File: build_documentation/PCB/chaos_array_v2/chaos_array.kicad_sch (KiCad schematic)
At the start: 26 parts, among them SW1 RotaryEncoder_Switch, SW2 SW_Push, SW3 RotaryEncoder_Switch, SW4 SW_Push, SW5 RotaryEncoder_Switch, SW6 SW_Push, SW7 RotaryEncoder_Switch, SW8 SW_Push, U1 RP2040-Zero

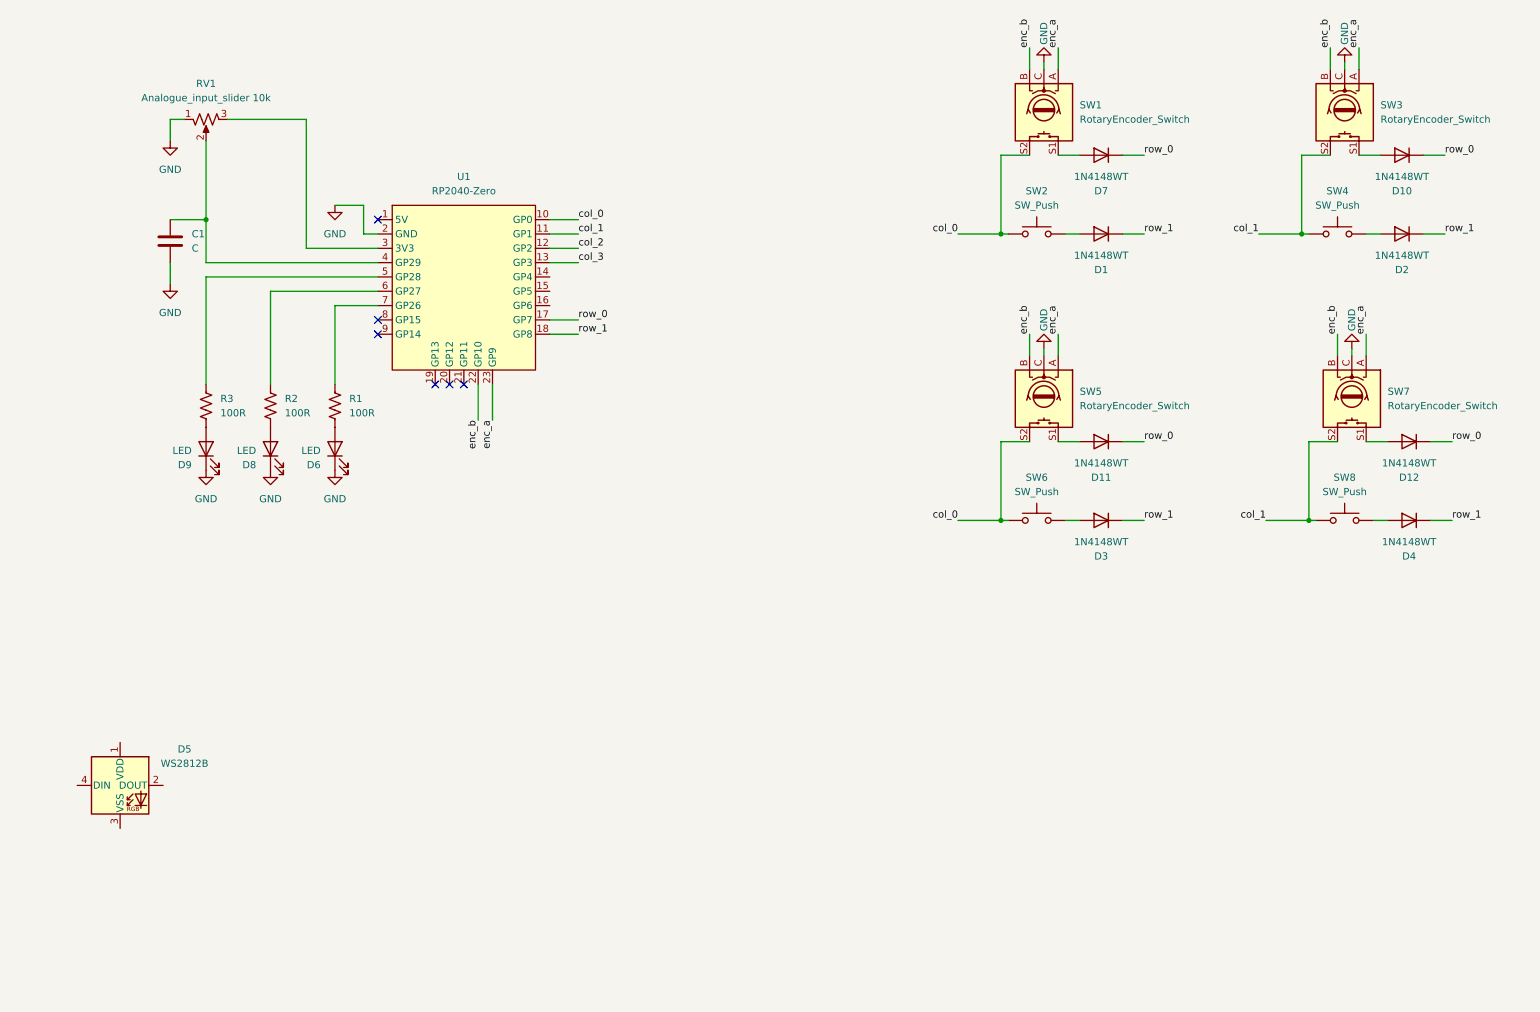
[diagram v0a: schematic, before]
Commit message: Create LED array and breakout area
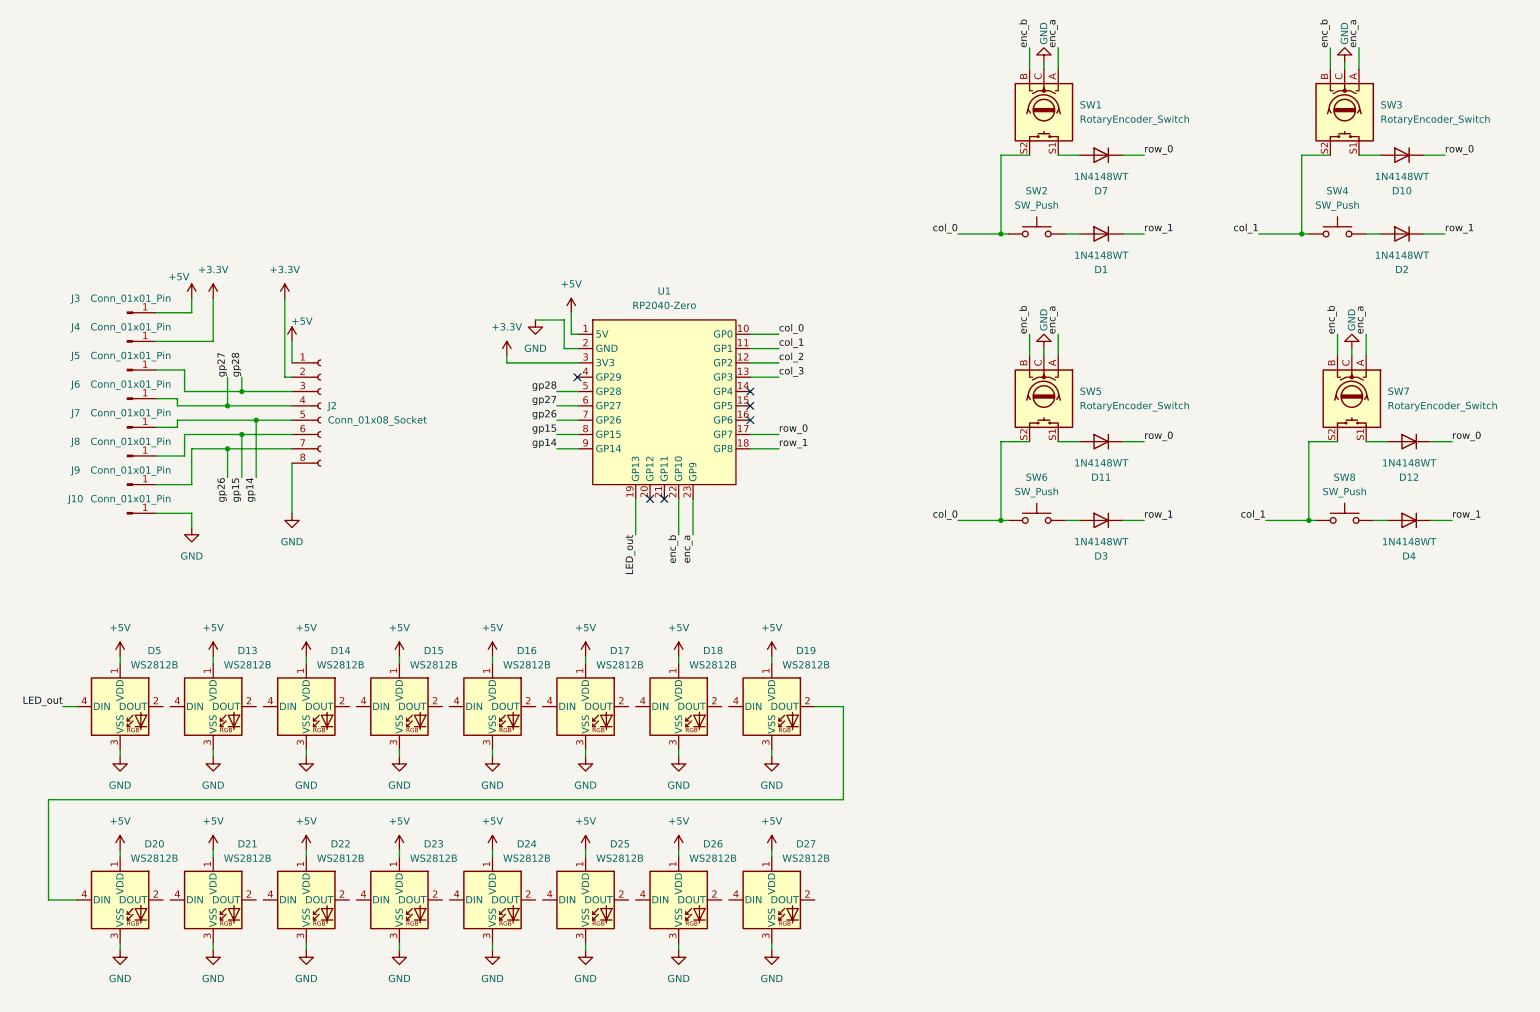
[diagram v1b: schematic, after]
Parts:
- removed C1: C, Capacitor_THT:C_Disc_D5.0mm_W2.5mm_P5.00mm, symbol Device:C
- removed D6, D8, D9: LED, LED_THT:LED_D3.0mm, symbol Device:LED
- removed R1, R2, R3: 100R, Resistor_THT:R_Axial_DIN0204_L3.6mm_D1.6mm_P5.08mm_Horizontal, symbol Device:R_US
- removed RV1: Analogue_input_slider 10k, CustomFootprints:Potentiometer_slide_75mm_range_60mm_2_sets, symbol Device:R_Potentiometer_US
- added D13, D14, D15, D16, D17, D18, D19, D20, D21, D22, D23, D24, D25, D26, D27: WS2812B, LED_SMD:LED_WS2812B_PLCC4_5.0x5.0mm_P3.2mm, symbol LED:WS2812B
- added J10, J3, J4, J5, J6, J7, J8, J9: Conn_01x01_Pin, symbol Connector:Conn_01x01_Pin
- added J2: Conn_01x08_Socket, Connector_JST:JST_EH_B8B-EH-A_1x08_P2.50mm_Vertical, symbol Connector:Conn_01x08_Socket
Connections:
- net GND: now also D5.3 (VSS), D13.3 (VSS), D14.3 (VSS), D15.3 (VSS), D16.3 (VSS), D17.3 (VSS), D18.3 (VSS), D19.3 (VSS), D20.3 (VSS), D21.3 (VSS), D22.3 (VSS), D23.3 (VSS), D24.3 (VSS), D25.3 (VSS), D26.3 (VSS), D27.3 (VSS), J10.1 (Pin_1), J2.8 (Pin_8)
- net +5V: now reaches U1.1 (5V)
- net +5V: now also D5.1 (VDD), D13.1 (VDD), D14.1 (VDD), D15.1 (VDD), D16.1 (VDD), D17.1 (VDD), D18.1 (VDD), D19.1 (VDD), D20.1 (VDD), D21.1 (VDD), D22.1 (VDD), D23.1 (VDD), D24.1 (VDD), D25.1 (VDD), D26.1 (VDD), D27.1 (VDD), J2.1 (Pin_1), J3.1 (Pin_1)
- net LED_out: now reaches U1.19 (GP13)
- net LED_out: now also D5.4 (DIN)
- net +3.3V: now reaches U1.3 (3V3)
- net +3.3V: now also J2.2 (Pin_2), J4.1 (Pin_1)
- net gp28: now reaches U1.5 (GP28)
- net gp28: now also J2.3 (Pin_3), J5.1 (Pin_1)
- net gp27: now reaches U1.6 (GP27)
- net gp27: now also J2.4 (Pin_4), J6.1 (Pin_1)
- net gp26: now reaches U1.7 (GP26)
- net gp26: now also J2.7 (Pin_7), J9.1 (Pin_1)
- net gp15: now reaches U1.8 (GP15)
- net gp15: now also J2.6 (Pin_6), J8.1 (Pin_1)
- net gp14: now reaches U1.9 (GP14)
- net gp14: now also J2.5 (Pin_5), J7.1 (Pin_1)
- new net: D19.2 (DOUT), D20.4 (DIN)
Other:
- moved on the sheet: D5, U1

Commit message: update BOM
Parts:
- D1, D10, D11, D2, D3, D4, D7: footprint Key_Switches:D_DO-35_SOD27_P5.08mm_Horizontal -> Diode_SMD:D_MiniMELF
- D5: renamed from D12; footprint Key_Switches:D_DO-35_SOD27_P5.08mm_Horizontal -> Diode_SMD:D_MiniMELF
- J10, J3, J4, J5, J6, J7, J8, J9: footprint (none) -> TestPoint:TestPoint_Pad_3.0x3.0mm
- renumbered D5 to D12
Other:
- note added: "WLED_array"
- note added: "breakout_area"
- note added: "switches_rotaries"
- moved on the sheet: D1, D10, D11, D12, D13, D14, D15, D16, D17, D18, D19, D2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

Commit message: Update footprints
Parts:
- SW2, SW4, SW6, SW8: footprint Key_Switches:Kailh_socket_MX_PG1350_optional -> footprints:Kailh_socket_MX_PG1350_optional
- U1: footprint CustomFootprints:RP2040 Zero -> RP2040 Zero:RP2040 Zero
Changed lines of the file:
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@@
 			)
 		)
-		(property "Footprint" "Key_Switches:Kailh_socket_MX_PG1350_optional"
+		(property "Footprint" "footprints:Kailh_socket_MX_PG1350_optional"
 			(at 251.46 147.32 0)
 			(hide yes)
@@
 			)
 		)
-		(property "Footprint" "CustomFootprints:RP2040 Zero"
+		(property "Footprint" "RP2040 Zero:RP2040 Zero"
 			(at 138.43 50.8 0)
 			(hide yes)
@@
 			)
 		)
-		(property "Footprint" "Key_Switches:Kailh_socket_MX_PG1350_optional"
+		(property "Footprint" "footprints:Kailh_socket_MX_PG1350_optional"
 			(at 196.85 147.32 0)
 			(hide yes)
@@
 			)
 		)
-		(property "Footprint" "Key_Switches:Kailh_socket_MX_PG1350_optional"
+		(property "Footprint" "footprints:Kailh_socket_MX_PG1350_optional"
 			(at 196.85 96.52 0)
 			(hide yes)
@@
 			)
 		)
-		(property "Footprint" "Key_Switches:Kailh_socket_MX_PG1350_optional"
+		(property "Footprint" "footprints:Kailh_socket_MX_PG1350_optional"
 			(at 250.19 96.52 0)
 			(hide yes)

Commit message: Routing
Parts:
- added C1: C_Polarized, Capacitor_SMD:CP_Elec_6.3x5.8, symbol Device:C_Polarized
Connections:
- net +5V: now also C1.1
- net GND: now also C1.2
- net LED_out: now also U1.4 (GP29); no longer U1.19 (GP13)
- net col_0: now also U1.12 (GP2); no longer SW5.S2, SW6.1, U1.10 (GP0)
- net col_1: now also U1.13 (GP3); no longer SW7.S2, SW8.1, U1.11 (GP1)
- net col_2: now also SW5.S2, SW6.1, U1.14 (GP4); no longer U1.12 (GP2)
- net col_3: now also SW7.S2, SW8.1, U1.15 (GP5); no longer U1.13 (GP3)
- net enc_a: now also U1.20 (GP12); no longer SW3.A, SW5.A, SW7.A, U1.23 (GP9)
- net enc_b: now also U1.19 (GP13); no longer SW3.B, SW5.B, SW7.B, U1.22 (GP10)
- net gp14: now also J2.7 (Pin_7), J9.1 (Pin_1); no longer J2.5 (Pin_5), J7.1 (Pin_1)
- net gp26: now also J2.5 (Pin_5), J7.1 (Pin_1); no longer J2.7 (Pin_7), J9.1 (Pin_1)
- net row_0: now also U1.11 (GP1); no longer U1.17 (GP7)
- net row_1: now also U1.10 (GP0); no longer U1.18 (GP8)
- net at D21.2 (DOUT): now also D22.4 (DIN)
- net at D21.4 (DIN): now also D20.2 (DOUT)
- net at D25.2 (DOUT): now also D26.4 (DIN)
- net at D25.4 (DIN): now also D24.2 (DOUT)
- net at D14.2 (DOUT): now also D15.4 (DIN)
- net at D14.4 (DIN): now also D13.2 (DOUT)
- net enc_g: now reaches U1.16 (GP6)
- net enc_g: now also SW7.A
- net enc_d: now reaches U1.21 (GP11)
- net enc_d: now also SW3.B
- net at D19.4 (DIN): now also D18.2 (DOUT)
- net at D24.4 (DIN): now also D23.2 (DOUT)
- net at D16.2 (DOUT): now also D17.4 (DIN)
- net at D16.4 (DIN): now also D15.2 (DOUT)
- net at D23.4 (DIN): now also D22.2 (DOUT)
- net at D26.2 (DOUT): now also D27.4 (DIN)
- net at D17.2 (DOUT): now also D18.4 (DIN)
- net at D12.2 (DOUT): now also D13.4 (DIN)
- new net enc_c: SW3.A, U1.22 (GP10)
- new net enc_e: SW5.A, U1.18 (GP8)
- new net enc_f: SW5.B, U1.23 (GP9)
- new net enc_h: SW7.B, U1.17 (GP7)
- no-connect marks 6 -> 0
